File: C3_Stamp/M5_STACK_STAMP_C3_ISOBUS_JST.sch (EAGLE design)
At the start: 3 parts, among them J1 61300811121, J2 61300611121

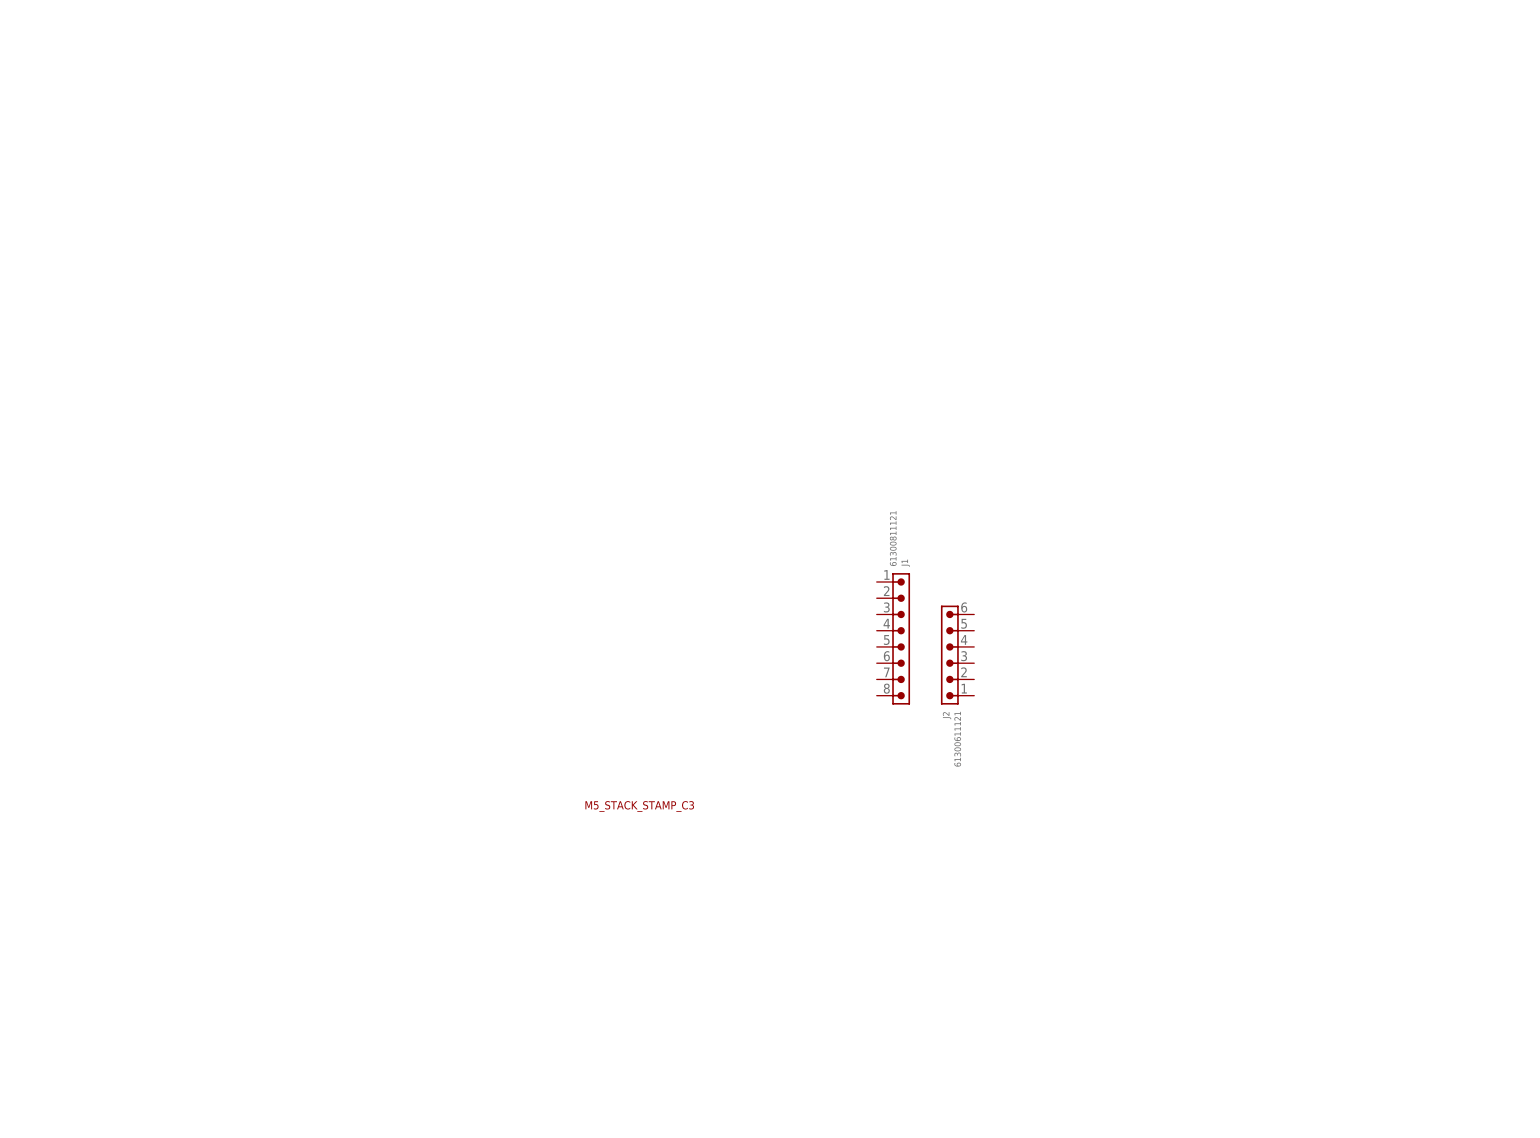
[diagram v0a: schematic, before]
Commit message: 2 different Connectors.
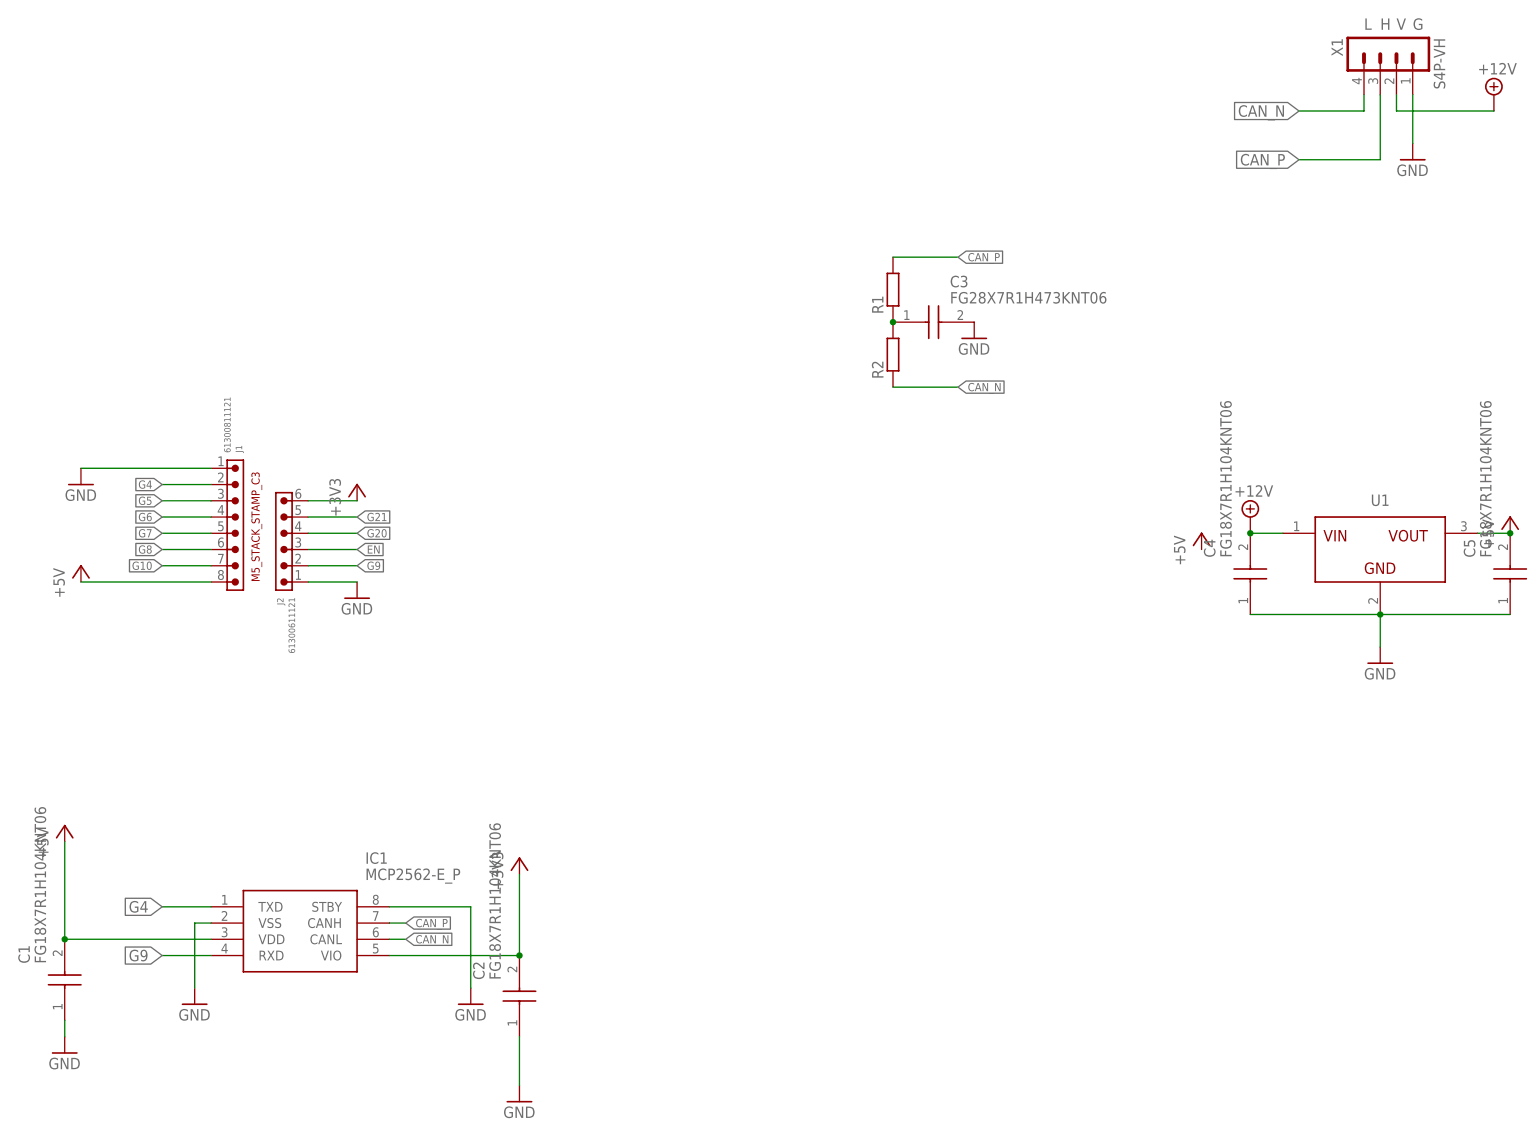
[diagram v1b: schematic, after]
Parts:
- added C1, C2, C4, C5: FG18X7R1H104KNT06, FG18X7R1H104KNT06-pcb-part-libraries:FG18X7R1H104KNT06
- added C3: FG28X7R1H473KNT06, FG28X7R1H473KNT06-pcb-part-libraries:FG28X7R1H473KNT06
- added IC1: MCP2562-E_P, MCP2562-E_P-pcb-part-libraries:MCP2562-E_P
- added R1, R2: (no value), resistor:R-EU_0204/7
- added U1: (no value), Wurth_Step Down Converter_MagI³C-FDSM:MAGI³C-FDSM_SIP-3_173010542_173XXXX42
- added X1: S4P-VH, con-JST VH:S4P-VH
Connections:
- new net +12V: C4.2, U1.VIN, X1.2
- new net +3V3: C2.2, IC1.VIO, J2.6
- new net +5V: C1.2, C5.2, IC1.VDD, J1.8, U1.VOUT
- new net CAN_N: IC1.CANL, R2.1, X1.4
- new net CAN_P: IC1.CANH, R1.2, X1.3
- new net EN: J2.3
- new net G10: J1.7
- new net G20: J2.4
- new net G21: J2.5
- new net G4: IC1.TXD, J1.2
- new net G5: J1.3
- new net G6: J1.4
- new net G7: J1.5
- new net G8: J1.6
- new net G9: IC1.RXD, J2.2
- new net GND: C1.1, C2.1, C3.2, C4.1, C5.1, IC1.STBY, IC1.VSS, J1.1, J2.1, U1.GND, X1.1
- new net N$1: C3.1, R1.1, R2.2
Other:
- note added: "G"
- note added: "H"
- note added: "L"
- note added: "V"
- moved on the sheet: J1, J2

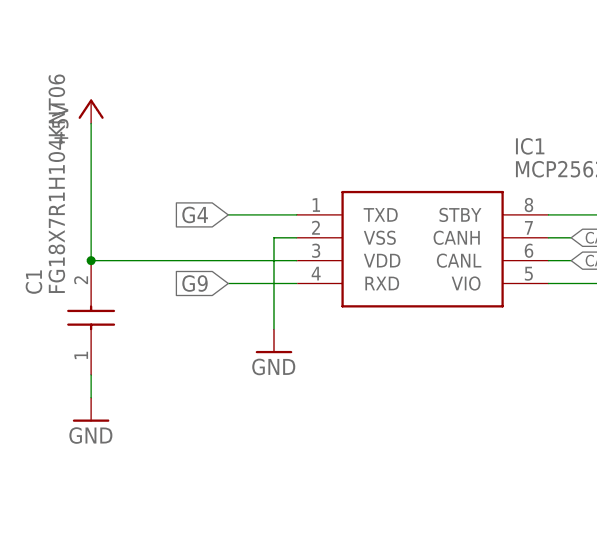
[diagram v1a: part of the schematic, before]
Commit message: G7 for CAN RX, as G9 is a Strapping Pin.
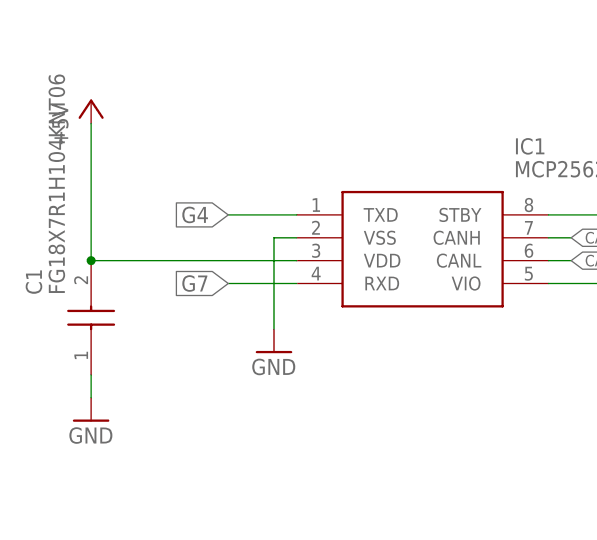
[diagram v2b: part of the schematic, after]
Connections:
- net G7: now also IC1.RXD
- net G9: no longer IC1.RXD
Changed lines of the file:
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@@
 <label x="25.4" y="86.36" size="1.27" layer="95" xref="yes"/>
-</segment>
-<segment>
-<pinref part="IC1" gate="G$1" pin="RXD"/>
-<wire x1="2.54" y1="25.4" x2="-5.08" y2="25.4" width="0.1524" layer="91"/>
-<label x="-5.08" y="25.4" size="1.778" layer="95" rot="R180" xref="yes"/>
 </segment>
 </net>
@@
 <label x="-5.08" y="91.44" size="1.27" layer="95" rot="R180" xref="yes"/>
 </segment>
+<segment>
+<pinref part="IC1" gate="G$1" pin="RXD"/>
+<wire x1="2.54" y1="25.4" x2="-5.08" y2="25.4" width="0.1524" layer="91"/>
+<label x="-5.08" y="25.4" size="1.778" layer="95" rot="R180" xref="yes"/>
+</segment>
 </net>
